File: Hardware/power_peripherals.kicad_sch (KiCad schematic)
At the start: 40 parts, among them J10 Conn_01x10, J11 Conn_01x10, J2 JST_2mm_LiPo, J3 Qwiic_RA, J7 Conn_01x10, J8 Conn_01x10, J9 microSD_Friction, U5 LM66200, U6 RT9080-3.3, U7 MCP73831, U8 MAX17048, U9 RT9080-3.3

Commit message: Finish v02 updates
Clean up schematic
Add test points for boot button and RGB LED output
Update pinouts of headers and RP2350
Fix pad shape of XBLR footprint
Finish routing
Update logos
Update jumper names
Add measures
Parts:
- removed C7, C8: 2.2uF, SparkFun-Capacitor:C_0603_1608Metric, symbol SparkFun-Capacitor:2.2uF_0603_10V_20%
- removed R24: 1k, SparkFun-Resistor:R_0603_1608Metric, symbol SparkFun-Resistor:1k_0603
- removed U9: RT9080-3.3, SparkFun-Semiconductor-Standard:SOT23-5, symbol SparkFun-Regulator:RT9080-3.3
- added C7: 0.1uF, SparkFun-Capacitor:C_0603_1608Metric, symbol SparkFun-Capacitor:0.1uF_0603_25V_20%
- added Q1: DMG2305UX, SparkFun-Semiconductor-Standard:SOT23-3, symbol SparkFun-DiscreteSemi:Q_PMOS_4.2A_20V
- added R14, R21, R24: 10k, SparkFun-Resistor:R_0603_1608Metric, symbol SparkFun-Resistor:10k_0603
- added SW1, SW2, SW4: SMD_4.6x2.8mm_h2.5mm, SparkFun-Switch:Push_SMD_4.6x2.8mm, symbol SparkFun-Switch:SPST_Push_SMD_4.6x2.8mm_h2.5mm
- added TP1, TP2: 1.0mm, SparkFun-Connector:TestPoint-1.0mm, symbol SparkFun-Connector:TestPoint_1.0mm
- J10, J11, J7, J8: footprint SparkFun-Connector:1x10 -> SparkFun-Connector:1x12; symbol SparkFun-Connector:Conn_01x10 -> SparkFun-Connector:Conn_01x12
- JP2: value ~ -> CHG
- JP3: value ~ -> PWR
- JP4: value ~ -> I2C
- JP7: value ~ -> LP
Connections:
- net RP2350_IO15 is gone; now on net RP2350_IO9: J11.3 (Pin_3)
- net RP2350_IO16 is gone; now on net RP2350_IO10: J11.2 (Pin_2)
- net RP2350_IO17 is gone; now on net RP2350_IO11: J11.1 (Pin_1)
- net RP2350_IO20 is gone; now on net GND: J10.1 (Pin_1)
- net RP2350_IO21 is gone; now on net VUSB: J10.2 (Pin_2)
- net 3.3V: now also J10.4 (Pin_4), R19.1, Q1.2 (S), R14.1, R21.1; no longer J10.7 (Pin_7), JP7.1 (A)
- net 3.3V_P: now also C7.1, Q1.3 (D)
- net GND: now also J10.12 (Pin_12), J11.12 (Pin_12), J7.1 (Pin_1), J7.12 (Pin_12), J8.1 (Pin_1), J8.12 (Pin_12), C7.2, R24.2, SW1.1, SW2.1, SW4.1; no longer J10.10 (Pin_10), J11.10 (Pin_10), R19.1
- net PERIPHERAL_POWER: now also JP7.2 (B), Q1.1 (G)
- net RP2350_IO10: no longer J11.8 (Pin_8)
- net RP2350_IO11: no longer J11.7 (Pin_7)
- net RP2350_IO26: now also J10.7 (Pin_7); no longer J10.3 (Pin_3)
- net RP2350_IO27: now also J10.8 (Pin_8); no longer J10.4 (Pin_4)
- net RP2350_IO28: now also J10.9 (Pin_9); no longer J10.5 (Pin_5)
- net RP2350_IO29: now also J10.10 (Pin_10); no longer J10.6 (Pin_6)
- net RP2350_IO9: no longer J11.9 (Pin_9)
- net VBATT: now also J10.3 (Pin_3); no longer J10.9 (Pin_9)
- net VUSB: no longer J10.8 (Pin_8)
- net XBLR_IO0: now also J8.2 (Pin_2); no longer J8.1 (Pin_1)
- net XBLR_IO1: now also J8.3 (Pin_3); no longer J8.2 (Pin_2)
- net XBLR_IO10: now also J7.11 (Pin_11); no longer J7.10 (Pin_10)
- net XBLR_IO11: now also J7.10 (Pin_10); no longer J7.9 (Pin_9)
- net XBLR_IO12: now also J7.9 (Pin_9); no longer J7.8 (Pin_8)
- net XBLR_IO15: now also J7.6 (Pin_6); no longer J7.5 (Pin_5)
- net XBLR_IO16: now also J7.5 (Pin_5); no longer J7.4 (Pin_4)
- net XBLR_IO17: now also J7.4 (Pin_4); no longer J7.3 (Pin_3)
- net XBLR_IO18: now also J7.3 (Pin_3); no longer J7.2 (Pin_2)
- net XBLR_IO19: now also J7.2 (Pin_2); no longer J7.1 (Pin_1)
- net XBLR_IO2: now also J8.4 (Pin_4); no longer J8.3 (Pin_3)
- net XBLR_IO3: now also J8.5 (Pin_5); no longer J8.4 (Pin_4)
- net XBLR_IO4: now also J8.6 (Pin_6); no longer J8.5 (Pin_5)
- net XBLR_IO5: now also J8.7 (Pin_7); no longer J8.6 (Pin_6)
- net XBLR_IO6: now also J8.8 (Pin_8); no longer J8.7 (Pin_7)
- net XBLR_IO7: now also J8.9 (Pin_9); no longer J8.8 (Pin_8)
- net XBLR_IO8: now also J8.10 (Pin_10); no longer J8.9 (Pin_9)
- net XBLR_IO9: now also J8.11 (Pin_11); no longer J8.10 (Pin_10)
- net XBLR_RX/IO14: now also J7.7 (Pin_7); no longer J7.6 (Pin_6)
- net XBLR_TX/IO13: now also J7.8 (Pin_8); no longer J7.7 (Pin_7)
- net ~{ON}: now also J10.5 (Pin_5)
- net LED_OUT: no longer names the net of D1.1 (DOUT)
- net LED_OUT: now also TP1.1
- net RP2350_IO12 renamed RP2350_IO6
- net RP2350_IO13 renamed RP2350_IO7
- net RP2350_IO14 renamed RP2350_IO8
- net VIN: no longer names the net of C1.1, U5.2 (VOUT), U5.7 (VOUT), U6.1 (VIN), U6.3 (EN)
- new net: JP7.1 (A), R24.1
- new net RP2350_IO1: J11.11 (Pin_11)
- new net RP2350_IO2: J11.10 (Pin_10)
- new net RP2350_IO3: J11.9 (Pin_9)
- new net RP2350_IO4: J11.8 (Pin_8)
- new net RP2350_IO5: J11.7 (Pin_7)
- new net USER_BUTTON: R21.2, SW4.2
- new net VDDA: J10.11 (Pin_11)
- new net ~{BOOT}: SW1.2, TP2.1
- new net ~{RESET}: J10.6 (Pin_6), R14.2, SW2.2
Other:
- note added: "!!! WARNING !!! Do not drive uSD card pins high if card is not powered, otherwise damage could occur!"
- note added: "Battery Charger - MCP73831"
- note added: "Battery Fuel Gauge - MAX17048"
- note added: "Buttons"
- note added: "Cut LP trace to make uSD card and RGB LED powered off by default"
- note removed: "Battery Charger"
- note removed: "Battery Fuel Gauge"
- note removed: "Cut LP trace to disable peripheral power by default"
- moved on the sheet: C1, C2, C26, C3, C4, C5, C6, D1, D2, D3, J2, J3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

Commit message: Re-annotate schematic
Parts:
- renumbered C1 to C24, C3 to C25, C2 to C27, C4 to C28, C5 to C29, C7 to C30, C6 to C31, D1 to D4, D3 to D5, D2 to D6, J9 to J10, J3 to J11, J10 to J5, J7 to J6, J11 to J7, J2 to J9, JP7 to JP4, JP2 to JP5, JP3 to JP6, JP4 to JP7, R8 to R15, R7 to R16, R19 to R17, R24 to R18, R9 to R19, R10 to R20, R11 to R21, R21 to R22, R5 to R23, R26 to R24, R14 to R25, R13 to R26, R20 to R27, R6 to R28, SW4 to SW2, SW2 to SW3, SW1 to SW4, U5 to U6, U6 to U7, U7 to U8, U8 to U9

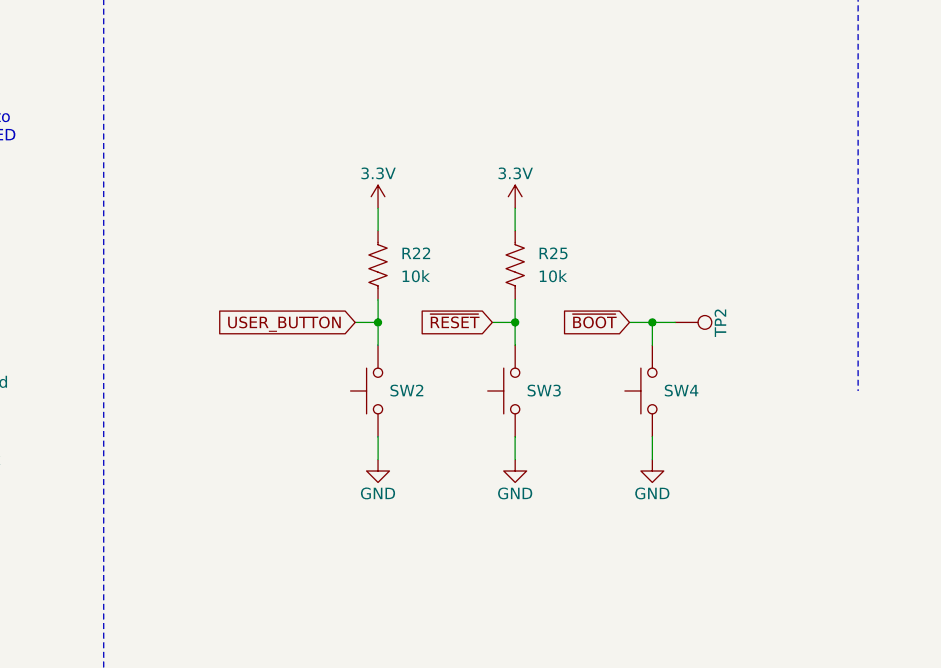
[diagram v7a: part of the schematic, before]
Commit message: Design review updates
Fix typo in USB calculations
Space out buttons in schematic
Add courtyard to flash memory
Reposition measures outside of enclosure outline
Reposition LEd silk outside of light pipe footprint
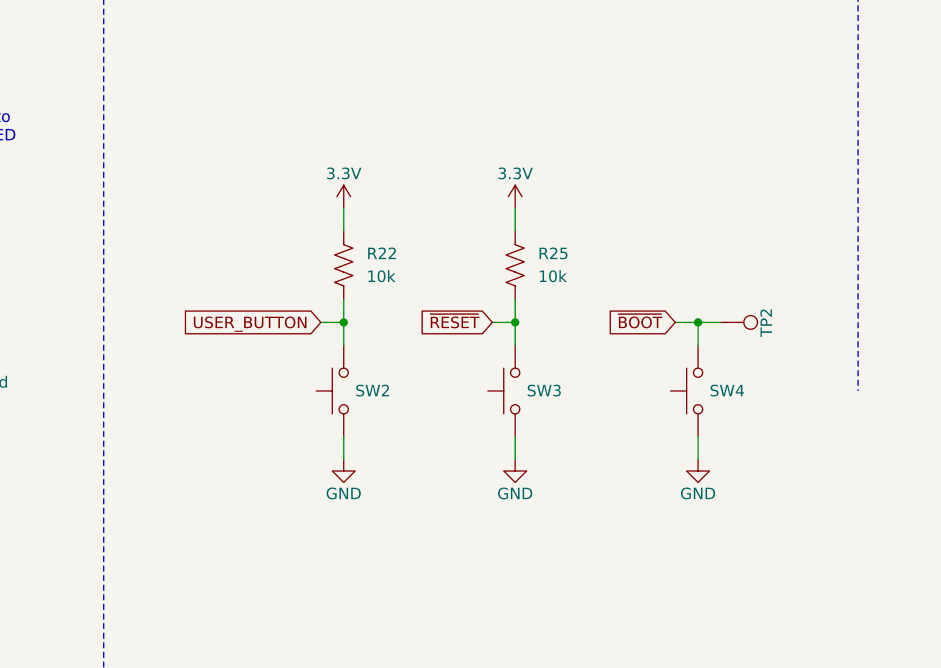
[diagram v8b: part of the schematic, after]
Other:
- moved on the sheet: R22, SW2, SW4, TP2
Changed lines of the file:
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@@
 	)
 	(junction
-		(at 259.08 226.06)
+		(at 255.27 226.06)
 		(diameter 0)
 		(color 0 0 0 0)
@@
 	)
 	(junction
-		(at 289.56 226.06)
+		(at 294.64 226.06)
 		(diameter 0)
 		(color 0 0 0 0)
@@
 	(wire
 		(pts
-			(xy 287.02 226.06) (xy 289.56 226.06)
+			(xy 292.1 226.06) (xy 294.64 226.06)
 		)
 		(stroke
@@
 	(wire
 		(pts
-			(xy 256.54 226.06) (xy 259.08 226.06)
+			(xy 252.73 226.06) (xy 255.27 226.06)
 		)
 		(stroke
@@
 	(wire
 		(pts
-			(xy 289.56 226.06) (xy 292.1 226.06)
+			(xy 294.64 226.06) (xy 297.18 226.06)
 		)
 		(stroke
@@
 	(wire
 		(pts
-			(xy 259.08 223.52) (xy 259.08 226.06)
+			(xy 255.27 223.52) (xy 255.27 226.06)
 		)
 		(stroke
@@
 	(wire
 		(pts
-			(xy 289.56 226.06) (xy 289.56 228.6)
+			(xy 294.64 226.06) (xy 294.64 228.6)
 		)
 		(stroke
@@
 	(wire
 		(pts
-			(xy 259.08 241.3) (xy 259.08 238.76)
+			(xy 255.27 241.3) (xy 255.27 238.76)
 		)
 		(stroke
@@
 	(wire
 		(pts
-			(xy 289.56 238.76) (xy 289.56 241.3)
+			(xy 294.64 238.76) (xy 294.64 241.3)
 		)
 		(stroke
@@
 	(wire
 		(pts
-			(xy 259.08 226.06) (xy 259.08 228.6)
+			(xy 255.27 226.06) (xy 255.27 228.6)
 		)
 		(stroke
@@
 	(wire
 		(pts
-			(xy 259.08 213.36) (xy 259.08 215.9)
+			(xy 255.27 213.36) (xy 255.27 215.9)
 		)
 		(stroke
@@
 	(global_label "USER_BUTTON"
 		(shape input)
-		(at 256.54 226.06 180)
+		(at 252.73 226.06 180)
 		(fields_autoplaced yes)
 		(effects
@@
 		)
 		(property "Intersheetrefs" "${INTERSHEET_REFS}"
-			(at 240.4315 226.06 0)
+			(at 236.6215 226.06 0)
 			(effects
 				(font
@@
 	(global_label "~{BOOT}"
 		(shape input)
-		(at 287.02 226.06 180)
+		(at 292.1 226.06 180)
 		(fields_autoplaced yes)
 		(effects
@@
 		)
 		(property "Intersheetrefs" "${INTERSHEET_REFS}"
-			(at 279.1362 226.06 0)
+			(at 284.2162 226.06 0)
 			(effects
 				(font
@@
 	(symbol
 		(lib_id "SparkFun-Resistor:10k_0603")
-		(at 259.08 219.71 90)
+		(at 255.27 219.71 90)
 		(unit 1)
 		(exclude_from_sim no)
@@
 		(fields_autoplaced yes)
 		(property "Reference" "R22"
-			(at 261.62 218.4399 90)
+			(at 257.81 218.4399 90)
 			(effects
 				(font
@@
 		)
 		(property "Value" "10k"
-			(at 261.62 220.9799 90)
+			(at 257.81 220.9799 90)
 			(effects
 				(font
@@
 		)
 		(property "Footprint" "SparkFun-Resistor:R_0603_1608Metric"
-			(at 263.398 219.71 0)
+			(at 259.588 219.71 0)
 			(effects
 				(font
@@
 		)
 		(property "Datasheet" "https://www.vishay.com/docs/20035/dcrcwe3.pdf"
-			(at 267.97 219.71 0)
+			(at 264.16 219.71 0)
 			(effects
 				(font
@@
 		)
 		(property "Description" "Resistor"
-			(at 270.51 219.71 0)
+			(at 266.7 219.71 0)
 			(effects
 				(font
@@
 		)
 		(property "PROD_ID" "RES-00824"
-			(at 265.43 219.71 0)
+			(at 261.62 219.71 0)
 			(effects
 				(font
@@
 	(symbol
 		(lib_id "SparkFun-PowerSymbol:3.3V")
-		(at 259.08 213.36 0)
+		(at 255.27 213.36 0)
 		(unit 1)
 		(exclude_from_sim no)
@@
 		(fields_autoplaced yes)
 		(property "Reference" "#PWR0114"
-			(at 259.08 217.17 0)
+			(at 255.27 217.17 0)
 			(effects
 				(font
@@
 		)
 		(property "Value" "3.3V"
-			(at 259.08 209.55 0)
+			(at 255.27 209.55 0)
 			(do_not_autoplace yes)
 			(effects
@@
 		)
 		(property "Footprint" ""
-			(at 259.08 213.36 0)
+			(at 255.27 213.36 0)
 			(effects
 				(font
@@
 		)
 		(property "Datasheet" ""
-			(at 259.08 213.36 0)
+			(at 255.27 213.36 0)
 			(effects
 				(font
@@
 		)
 		(property "Description" "Power symbol creates a global label with name \"3.3V\""
-			(at 259.08 213.36 0)
+			(at 255.27 213.36 0)
 			(effects
 				(font
@@
 	(symbol
 		(lib_id "SparkFun-Switch:SPST_Push_SMD_4.6x2.8mm_h2.5mm")
-		(at 289.56 233.68 90)
+		(at 294.64 233.68 90)
 		(unit 1)
 		(exclude_from_sim no)
@@
 		(fields_autoplaced yes)
 		(property "Reference" "SW4"
-			(at 290.83 233.6799 90)
+			(at 295.91 233.6799 90)
 			(effects
 				(font
@@
 		)
 		(property "Value" "SMD_4.6x2.8mm_h2.5mm"
-			(at 290.83 234.9499 90)
+			(at 295.91 234.9499 90)
 			(effects
 				(font
@@
 		)
 		(property "Footprint" "SparkFun-Switch:Push_SMD_4.6x2.8mm"
-			(at 294.64 233.68 0)
+			(at 299.72 233.68 0)
 			(effects
 				(font
@@
 		)
 		(property "Datasheet" "~"
-			(at 299.72 233.68 0)
+			(at 304.8 233.68 0)
 			(effects
 				(font
@@
 		)
 		(property "Description" "Single Pole Single Throw (SPST) switch"
-			(at 289.56 233.68 0)
+			(at 294.64 233.68 0)
 			(effects
 				(font
@@
 		)
 		(property "PROD_ID" "SWCH-15606"
-			(at 297.18 233.68 0)
+			(at 302.26 233.68 0)
 			(effects
 				(font
@@
 	(symbol
 		(lib_id "SparkFun-PowerSymbol:GND")
-		(at 289.56 241.3 0)
+		(at 294.64 241.3 0)
 		(unit 1)
 		(exclude_from_sim no)
@@
 		(fields_autoplaced yes)
 		(property "Reference" "#PWR0124"
-			(at 289.56 247.65 0)
+			(at 294.64 247.65 0)
 			(effects
 				(font
@@
 		)
 		(property "Value" "GND"
-			(at 289.56 245.11 0)
+			(at 294.64 245.11 0)
 			(do_not_autoplace yes)
 			(effects
@@
 		)
 		(property "Footprint" ""
-			(at 289.56 241.3 0)
+			(at 294.64 241.3 0)
 			(effects
 				(font
@@
 		)
 		(property "Datasheet" ""
-			(at 289.56 241.3 0)
+			(at 294.64 241.3 0)
 			(effects
 				(font
@@
 		)
 		(property "Description" "Power symbol creates a global label with name \"GND\" , ground"
-			(at 289.56 241.3 0)
+			(at 294.64 241.3 0)
 			(effects
 				(font
@@
 	(symbol
 		(lib_id "SparkFun-Switch:SPST_Push_SMD_4.6x2.8mm_h2.5mm")
-		(at 259.08 233.68 90)
+		(at 255.27 233.68 90)
 		(unit 1)
 		(exclude_from_sim no)
@@
 		(fields_autoplaced yes)
 		(property "Reference" "SW2"
-			(at 260.35 233.6799 90)
+			(at 256.54 233.6799 90)
 			(effects
 				(font
@@
 		)
 		(property "Value" "SMD_4.6x2.8mm_h2.5mm"
-			(at 260.35 234.9499 90)
+			(at 256.54 234.9499 90)
 			(effects
 				(font
@@
 		)
 		(property "Footprint" "SparkFun-Switch:Push_SMD_4.6x2.8mm"
-			(at 264.16 233.68 0)
+			(at 260.35 233.68 0)
 			(effects
 				(font
@@
 		)
 		(property "Datasheet" "~"
-			(at 269.24 233.68 0)
+			(at 265.43 233.68 0)
 			(effects
 				(font
@@
 		)
 		(property "Description" "Single Pole Single Throw (SPST) switch"
-			(at 259.08 233.68 0)
+			(at 255.27 233.68 0)
 			(effects
 				(font
@@
 		)
 		(property "PROD_ID" "SWCH-15606"
-			(at 266.7 233.68 0)
+			(at 262.89 233.68 0)
 			(effects
 				(font
@@
 	(symbol
 		(lib_id "SparkFun-Connector:TestPoint_1.0mm")
-		(at 292.1 226.06 270)
+		(at 297.18 226.06 270)
 		(unit 1)
 		(exclude_from_sim no)
@@
 		(fields_autoplaced yes)
 		(property "Reference" "TP2"
-			(at 297.18 226.06 0)
+			(at 302.26 226.06 0)
 			(do_not_autoplace yes)
 			(effects
@@
 		)
 		(property "Value" "1.0mm"
-			(at 288.29 226.06 0)
+			(at 293.37 226.06 0)
 			(effects
 				(font
@@
 		)
 		(property "Footprint" "SparkFun-Connector:TestPoint-1.0mm"
-			(at 285.75 226.06 0)
+			(at 290.83 226.06 0)
 			(effects
 				(font
@@
 		)
 		(property "Datasheet" "~"
-			(at 284.48 226.06 0)
+			(at 289.56 226.06 0)
 			(effects
 				(font
@@
 		)
 		(property "Description" "Test Point"
-			(at 292.1 226.06 0)
+			(at 297.18 226.06 0)
 			(effects
 				(font
@@
 	(symbol
 		(lib_id "SparkFun-PowerSymbol:GND")
-		(at 259.08 241.3 0)
+		(at 255.27 241.3 0)
 		(unit 1)
 		(exclude_from_sim no)
@@
 		(fields_autoplaced yes)
 		(property "Reference" "#PWR0115"
-			(at 259.08 247.65 0)
+			(at 255.27 247.65 0)
 			(effects
 				(font
@@
 		)
 		(property "Value" "GND"
-			(at 259.08 245.11 0)
+			(at 255.27 245.11 0)
 			(do_not_autoplace yes)
 			(effects
@@
 		)
 		(property "Footprint" ""
-			(at 259.08 241.3 0)
+			(at 255.27 241.3 0)
 			(effects
 				(font
@@
 		)
 		(property "Datasheet" ""
-			(at 259.08 241.3 0)
+			(at 255.27 241.3 0)
 			(effects
 				(font
@@
 		)
 		(property "Description" "Power symbol creates a global label with name \"GND\" , ground"
-			(at 259.08 241.3 0)
+			(at 255.27 241.3 0)
 			(effects
 				(font
